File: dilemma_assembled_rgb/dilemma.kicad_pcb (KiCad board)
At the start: 2 copper layers, 106.1 x 95.1 mm, 104 parts, among them J1 USB_C_Receptacle_USB2.0, J102 Serial, J105 Conn_01x04_Female, J113 Cirque, J2 Conn_01x03_Female, J5 Conn_01x02, SW1 SW_Push, SW110 SW_SPST, SW2 SW_Push, SW3002 RotaryEncoder_Switch, U1 RP2040, U2 GD25Q80CEIGR, U3 XC6210B332MR-G, U4 USBLC6-2P6, Y1 Crystal_GND24

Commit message: cleanup
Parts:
- renumbered D36 to D47
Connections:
- D37 pad 1: Net-(D36-Pad3) -> Net-(D37-Pad1)
- D47 pad 1: Net-(D35-Pad3) -> Net-(D36-Pad3)
- D47 pad 3: Net-(D36-Pad3) -> Net-(D37-Pad1)

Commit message: rgb schem work
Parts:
- removed C1, C2: 1µ, Capacitor_SMD:C_0603_1608Metric
- removed C10, C11, C12, C13, C14, C7, C8, C9: 100n, Capacitor_SMD:C_0402_1005Metric
- removed C3, C4: 15p, Capacitor_SMD:C_0402_1005Metric
- removed C5, C6: 1µ, Capacitor_SMD:C_0402_1005Metric
- removed D1: LED, LED_SMD:LED_0402_1005Metric
- removed D19: NA_SK6805-hole, 0xB2_drawings:LED_SK6805-EC15_hole
- removed D2: B5817, Diode_SMD:D_SOD-323
- removed D22, D25, D28, D3: SK6805-EC15, 0xB2_drawings:LED_SK6805-EC15_hole
- removed F1: Polyfuse, Fuse:Fuse_0603_1608Metric
- removed FB1: FerriteBead_Small, Inductor_SMD:L_0603_1608Metric
- removed G*** (x3): LOGO, local-libraries:LOGO
- removed H102: M4, local-libraries:MountingHole_3mm_Pad_hole
- removed H103, H109, H110: t, local-libraries:JLC_SMT_Assembly_Hole
- removed H105, H106, H107, H108: M4, local-libraries:MountingHole_3mm_Pad_Via
- removed J102: Serial, local-libraries:Jack_3.5mm_PJ320E_Horizontal
- removed J105: Conn_01x04_Female, local-libraries:PinHeader_1x04_P2.54mm_Vertical_debug
- removed J113: Cirque, local-libraries:FPC-SMD_FPC05012-09200-.5mm
- removed J2: Conn_01x03_Female, Connector_PinHeader_2.54mm:PinHeader_1x03_P2.54mm_Vertical
- removed J2: Conn_01x03_Female, local-libraries:PinHeader_1x03_P2.54mm_Vertical_smd
- removed J5: Conn_01x02, Connector_PinHeader_1.27mm:PinHeader_1x02_P1.27mm_Vertical
- removed O101: OLED, local-libraries:PinHeader_1x04_P2.54mm_Vertical
- removed R1, R3, R8: 1k, Resistor_SMD:R_0402_1005Metric
- removed R10, R4, R5: 5.1k, Resistor_SMD:R_0402_1005Metric
- removed R101: 5.1k, local-libraries:R_0402_1005Metric_nolabel
- removed R103, R104: 4.7k, local-libraries:R_0402_1005Metric_nolabel
- removed R11, R2, R9: 10k, Resistor_SMD:R_0402_1005Metric
- removed R6, R7: 27, Resistor_SMD:R_0402_1005Metric
- removed REF**: OSHW-Logo_5.7x6mm_SilkScreen, Symbol:OSHW-Logo_5.7x6mm_SilkScreen
- removed SW1, SW2: SW_Push, Button_Switch_SMD:SW_SPST_CK_KXT3
- removed SW110: SW_SPST, local-libraries:SW_Push_1P1T_NO_6x6mm_H9.5mm
- removed U1: RP2040, 0xLib_Package_DFN_QFN:QFN-56-1EP_7x7mm_P0.4mm_EP3.2x3.2mm
- removed U2: GD25Q80CEIGR, 0xLib_Package_DFN_QFN:USON-8-1EP_3x2mm_P0.5mm_EP0.25x1.65mm
- removed U3: XC6210B332MR-G, Package_TO_SOT_SMD:SOT-23-5
- removed U4: USBLC6-2P6, Package_TO_SOT_SMD:SOT-666
- removed Y1: Crystal_GND24, Crystal:Crystal_SMD_2520-4Pin_2.5x2.0mm
- removed kibuzzard-61F01A92: G***, local-libraries:kibuzzard-61F01A92
- removed kibuzzard-62C19A64 (x2): G***, kibuzzard-62C19A64
- removed kibuzzard-62C19AB4: G***, kibuzzard-62C19AB4
- removed kibuzzard-62C19AC2: G***, kibuzzard-62C19AC2
- removed kibuzzard-62C5480E: G***, kibuzzard-62C5480E
- added D9: NA_SK6805-hole, 0xB2_drawings:LED_SK6805-EC15_hole, F.Cu at (126.8, 110.5)
- H101, H104: value M4 -> NA_M4
- H111: value t -> NA_t
- J1: value USB_C_Receptacle_USB2.0 -> NA_Conn_01x03_Female; footprint 0xLib_USB_Type-C:USB_C_Receptacle_HRO_TYPE-C-31-M-13B -> local-libraries:PinHeader_1x03_P2.54mm_Vertical_smd
- SW3002: value RotaryEncoder_Switch -> NA_RotaryEncoder_Switch
- moved J1 62.9 mm to (132.0, 91.0), turned to 0 degrees
- moved D8 1.10 mm to (91.2, 102.2)
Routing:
- net Net-(D43-Pad3): track 0.00 -> 89.5 mm, vias 0 -> 2
- net RGB: track 0.00 -> 51.2 mm, vias 0 -> 1
- net Net-(D34-Pad3): track 0.00 -> 31.7 mm
- net Net-(D44-Pad3): track 0.00 -> 28.5 mm
- net Net-(D38-Pad3): track 0.00 -> 27.5 mm
- net Net-(D35-Pad3): track 0.00 -> 25.7 mm
- net Net-(D37-Pad1): track 0.00 -> 25.1 mm
- net Net-(D42-Pad3): track 0.00 -> 24.8 mm
- net Net-(D37-Pad3): track 0.00 -> 24.7 mm
- net Net-(D45-Pad3): track 0.00 -> 24.7 mm
- net Net-(D33-Pad3): track 0.00 -> 24.5 mm
- net Net-(D36-Pad3): track 0.00 -> 24.3 mm
- net Net-(D41-Pad3): track 0.00 -> 20.7 mm
- net Net-(D32-Pad3): track 0.00 -> 19.8 mm
- net Net-(D40-Pad3): track 0.00 -> 19.0 mm
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- removed copper zone on F.Cu, net +3V3
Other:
- board text removed: "3V3"
- board text removed: "BastardKB x Freznel x plut0nium"
- board text removed: "CERN-OHL-S v2"
- board text removed: "GND"
- board text removed: "S"
- board text removed: "SWCLK"
- board text removed: "SWD"
- board text removed: "a2.0a"

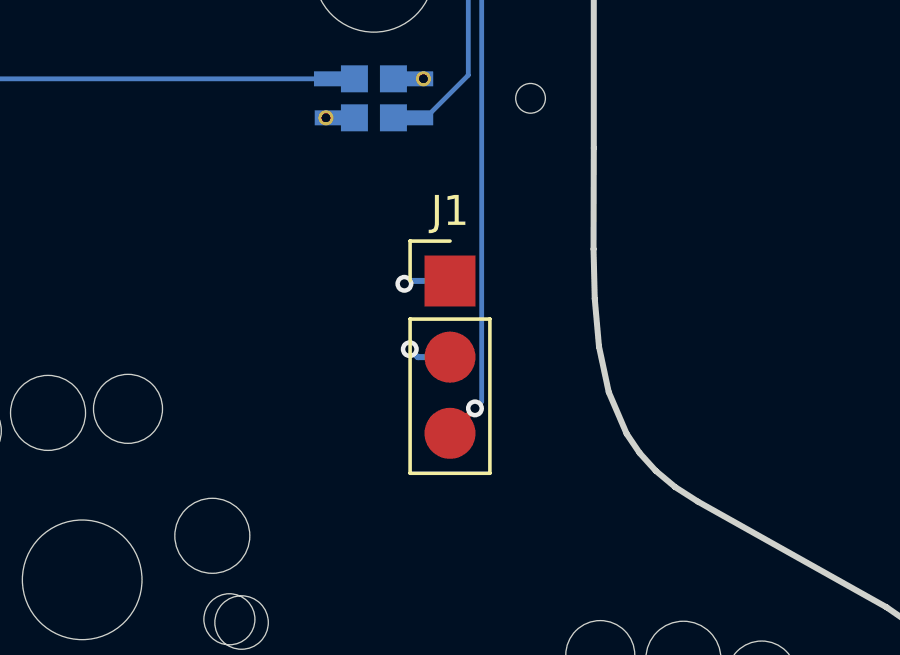
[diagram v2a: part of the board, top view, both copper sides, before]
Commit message: fix per key RGB connection
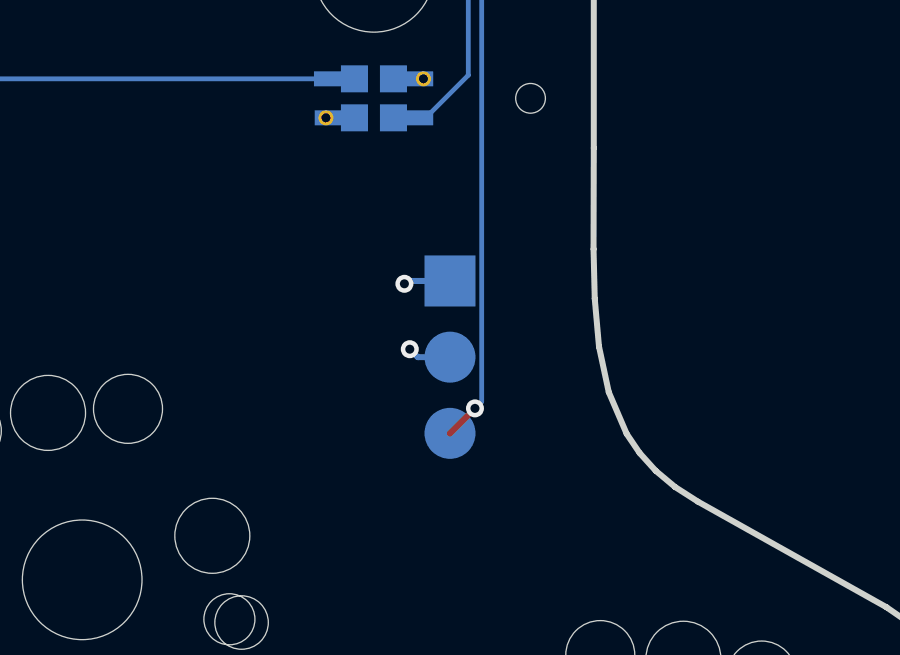
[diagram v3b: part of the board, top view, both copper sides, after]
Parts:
- J1: moved to B.Cu
- turned J1 to 180 degrees
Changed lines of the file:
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@@
     )
-  )
-  (footprint "local-libraries:PinHeader_1x03_P2.54mm_Vertical_smd" (layer "F.Cu")
-    (at 131.960135 91.035)
-    (descr "Through hole straight pin header, 1x03, 2.54mm pitch, single row")
-    (tags "Through hole pin header THT 1x03 2.54mm single row")
-    (property "Sheetfile" "dilemma.kicad_sch")
-    (property "Sheetname" "")
-    (attr through_hole)
-    (fp_text reference "J1" (at 0 -2.33) (layer "F.SilkS")
-      (effects (font (size 1 1) (thickness 0.15)))
-    )
-    (fp_text value "NA_Conn_01x03_Female" (at 0 7.41) (layer "F.Fab")
-      (effects (font (size 1 1) (thickness 0.15)))
-    )
-    (fp_text user "${REFERENCE}" (at 0 2.54 90) (layer "F.Fab")
-      (effects (font (size 1 1) (thickness 0.15)))
-    )
-    (fp_line (start 1.33 1.27) (end 1.33 6.41) (layer "F.SilkS") (width 0.12))
-    (fp_line (start -1.33 1.27) (end -1.33 6.41) (layer "F.SilkS") (width 0.12))
-    (fp_line (start -1.33 -1.33) (end 0 -1.33) (layer "F.SilkS") (width 0.12))
-    (fp_line (start -1.33 6.41) (end 1.33 6.41) (layer "F.SilkS") (width 0.12))
-    (fp_line (start -1.33 1.27) (end 1.33 1.27) (layer "F.SilkS") (width 0.12))
-    (fp_line (start -1.33 0) (end -1.33 -1.33) (layer "F.SilkS") (width 0.12))
-    (fp_line (start -1.8 6.85) (end 1.8 6.85) (layer "F.CrtYd") (width 0.05))
-    (fp_line (start 1.8 6.85) (end 1.8 -1.8) (layer "F.CrtYd") (width 0.05))
-    (fp_line (start -1.8 -1.8) (end -1.8 6.85) (layer "F.CrtYd") (width 0.05))
-    (fp_line (start 1.8 -1.8) (end -1.8 -1.8) (layer "F.CrtYd") (width 0.05))
-    (fp_line (start 1.27 6.35) (end -1.27 6.35) (layer "F.Fab") (width 0.1))
-    (fp_line (start 1.27 -1.27) (end 1.27 6.35) (layer "F.Fab") (width 0.1))
-    (fp_line (start -0.635 -1.27) (end 1.27 -1.27) (layer "F.Fab") (width 0.1))
-    (fp_line (start -1.27 -0.635) (end -0.635 -1.27) (layer "F.Fab") (width 0.1))
-    (fp_line (start -1.27 6.35) (end -1.27 -0.635) (layer "F.Fab") (width 0.1))
-    (pad "1" smd rect (at 0 0) (size 1.7 1.7) (layers "F.Cu" "F.Paste" "F.Mask")
-      (net 2 "GND") (pinfunction "Pin_1") (pintype "passive"))
-    (pad "2" smd oval (at 0 2.54) (size 1.7 1.7) (layers "F.Cu" "F.Paste" "F.Mask")
-      (net 4 "+3V3") (pinfunction "Pin_2") (pintype "passive"))
-    (pad "3" smd oval (at 0 5.08) (size 1.7 1.7) (layers "F.Cu" "F.Paste" "F.Mask")
-      (net 3 "RGB") (pinfunction "Pin_3") (pintype "passive"))
   )
   (footprint "0xB2_drawings:LED_SK6805-EC15_hole" (layer "F.Cu")
@@
     )
   )
-  (footprint "local-libraries:LED_SK6805-EC15_withSwitch" (layer "B.Cu")
+  (footprint "local-libraries:PinHeader_1x03_P2.54mm_Vertical_smd" (layer "B.Cu")
+    (at 131.960135 91.035 180)
+    (descr "Through hole straight pin header, 1x03, 2.54mm pitch, single row")
+    (tags "Through hole pin header THT 1x03 2.54mm single row")
+    (property "Sheetfile" "dilemma.kicad_sch")
+    (property "Sheetname" "")
+    (attr through_hole)
+    (fp_text reference "J1" (at 0 2.33) (layer "B.SilkS")
+      (effects (font (size 1 1) (thickness 0.15)) (justify mirror))
+    )
+    (fp_text value "NA_Conn_01x03_Female" (at 0 -7.41) (layer "B.Fab")
+      (effects (font (size 1 1) (thickness 0.15)) (justify mirror))
+    )
+    (fp_text user "${REFERENCE}" (at 0 -2.54 90) (layer "B.Fab")
+      (effects (font (size 1 1) (thickness 0.15)) (justify mirror))
+    )
+    (fp_line (start 1.33 -1.27) (end 1.33 -6.41) (layer "B.SilkS") (width 0.12))
+    (fp_line (start -1.33 -1.27) (end -1.33 -6.41) (layer "B.SilkS") (width 0.12))
+    (fp_line (start -1.33 1.33) (end 0 1.33) (layer "B.SilkS") (width 0.12))
+    (fp_line (start -1.33 -6.41) (end 1.33 -6.41) (layer "B.SilkS") (width 0.12))
+    (fp_line (start -1.33 -1.27) (end 1.33 -1.27) (layer "B.SilkS") (width 0.12))
+    (fp_line (start -1.33 0) (end -1.33 1.33) (layer "B.SilkS") (width 0.12))
+    (fp_line (start -1.8 -6.85) (end 1.8 -6.85) (layer "B.CrtYd") (width 0.05))
+    (fp_line (start 1.8 -6.85) (end 1.8 1.8) (layer "B.CrtYd") (width 0.05))
+    (fp_line (start -1.8 1.8) (end -1.8 -6.85) (layer "B.CrtYd") (width 0.05))
+    (fp_line (start 1.8 1.8) (end -1.8 1.8) (layer "B.CrtYd") (width 0.05))
+    (fp_line (start 1.27 -6.35) (end -1.27 -6.35) (layer "B.Fab") (width 0.1))
+    (fp_line (start 1.27 1.27) (end 1.27 -6.35) (layer "B.Fab") (width 0.1))
+    (fp_line (start -0.635 1.27) (end 1.27 1.27) (layer "B.Fab") (width 0.1))
+    (fp_line (start -1.27 0.635) (end -0.635 1.27) (layer "B.Fab") (width 0.1))
+    (fp_line (start -1.27 -6.35) (end -1.27 0.635) (layer "B.Fab") (width 0.1))
+    (pad "1" smd rect (at 0 0 180) (size 1.7 1.7) (layers "B.Cu" "B.Paste" "B.Mask")
+      (net 2 "GND") (pinfunction "Pin_1") (pintype "passive"))
+    (pad "2" smd oval (at 0 -2.54 180) (size 1.7 1.7) (layers "B.Cu" "B.Paste" "B.Mask")
+      (net 4 "+3V3") (pinfunction "Pin_2") (pintype "passive"))
+    (pad "3" smd oval (at 0 -5.08 180) (size 1.7 1.7) (layers "B.Cu" "B.Paste" "B.Mask")
+      (net 3 "RGB") (pinfunction "Pin_3") (pintype "passive"))
+  )
+  (footprint "local-libraries:LED_SK6805-EC15_withSwitch" (layer "B.Cu")

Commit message: bom
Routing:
- net RGB: track 51.2 -> 52.4 mm
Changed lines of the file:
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@@
     (property "Sheetfile" "dilemma.kicad_sch")
     (property "Sheetname" "")
-    (attr exclude_from_pos_files)
+    (attr exclude_from_pos_files exclude_from_bom)
     (fp_text reference "H101" (at 0 -3.7) (layer "F.SilkS") hide
       (effects (font (size 1 1) (thickness 0.15)))
@@
     (property "Sheetfile" "dilemma.kicad_sch")
     (property "Sheetname" "")
-    (attr through_hole exclude_from_pos_files)
+    (attr through_hole exclude_from_pos_files exclude_from_bom)
     (fp_text reference "H111" (at 7.6835 1.4605) (layer "F.Fab")
       (effects (font (size 1 1) (thickness 0.15)))
@@
     (property "Sheetfile" "dilemma.kicad_sch")
     (property "Sheetname" "")
-    (attr exclude_from_pos_files)
+    (attr exclude_from_pos_files exclude_from_bom)
     (fp_text reference "H104" (at 0 -3.7) (layer "F.SilkS") hide
       (effects (font (size 1 1) (thickness 0.15)))
@@
     (property "Sheetfile" "dilemma.kicad_sch")
     (property "Sheetname" "")
-    (attr through_hole)
+    (attr through_hole exclude_from_pos_files exclude_from_bom)
     (fp_text reference "J1" (at 0 2.33) (layer "B.SilkS")
       (effects (font (size 1 1) (thickness 0.15)) (justify mirror))
@@
     (property "Sheetfile" "dilemma.kicad_sch")
     (property "Sheetname" "")
-    (attr through_hole)
+    (attr through_hole exclude_from_pos_files exclude_from_bom)
     (fp_text reference "SW3002" (at 2.8 4.7 270) (layer "B.SilkS")
       (effects (font (size 1 1) (thickness 0.15)) (justify mirror))
@@
   (segment (start 131.960135 96.115) (end 131.960136 96.115) (width 0.2) (layer "F.Cu") (net 3))
   (via (at 132.792568 95.282568) (size 0.6) (drill 0.3) (layers "F.Cu" "B.Cu") (net 3))
+  (segment (start 131.960136 96.115) (end 132.792568 95.282568) (width 0.16) (layer "B.Cu") (net 3))
   (segment (start 131.705479 63.074521) (end 131.705479 48.753979) (width 0.16) (layer "B.Cu") (net 3))
   (segment (start 133.15 70.350958) (end 133.15 64.519042) (width 0.16) (layer "B.Cu") (net 3))
   (segment (start 131.705479 78.841049) (end 131.705479 71.795479) (width 0.16) (layer "B.Cu") (net 3))
   (segment (start 131.705479 71.795479) (end 133.15 70.350958) (width 0.16) (layer "B.Cu") (net 3))
+  (segment (start 131.960135 96.115) (end 131.960136 96.115) (width 0.16) (layer "B.Cu") (net 3))
   (segment (start 131.705479 48.753979) (end 130.549 47.5975) (width 0.16) (layer "B.Cu") (net 3))
   (segment (start 133.15 64.519042) (end 131.705479 63.074521) (width 0.16) (layer "B.Cu") (net 3))

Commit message: update bom
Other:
- board text added: "a2.0a_R"
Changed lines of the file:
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@@
   (gr_circle (center 89.51 86.41) (end 94.81 86.41) (layer "User.1") (width 0.15) (fill none))
   (gr_circle (center 69.11 30.67) (end 74.41 30.67) (layer "User.1") (width 0.15) (fill none))
+  (gr_text "a2.0a_R" (at 128.05 93.34 -90) (layer "B.SilkS")
+    (effects (font (size 1.2 1.2) (thickness 0.12)) (justify mirror))
+  )
   (segment (start 130.075 67.415) (end 130.075 66.5975) (width 0.16) (layer "B.Cu") (net 1))
   (segment (start 129.72 67.77) (end 130.075 67.415) (width 0.16) (layer "B.Cu") (net 1))
